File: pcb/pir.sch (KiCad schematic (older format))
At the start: 0 parts

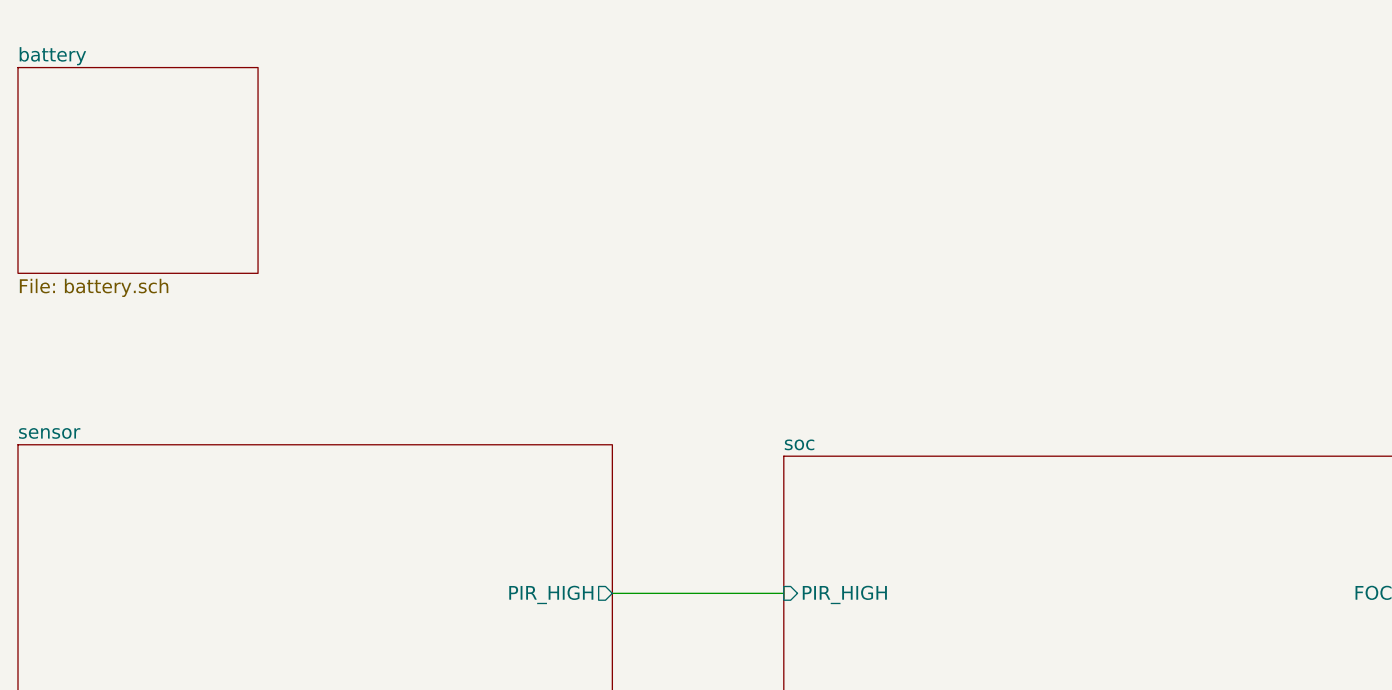
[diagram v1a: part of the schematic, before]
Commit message: User pushbutton
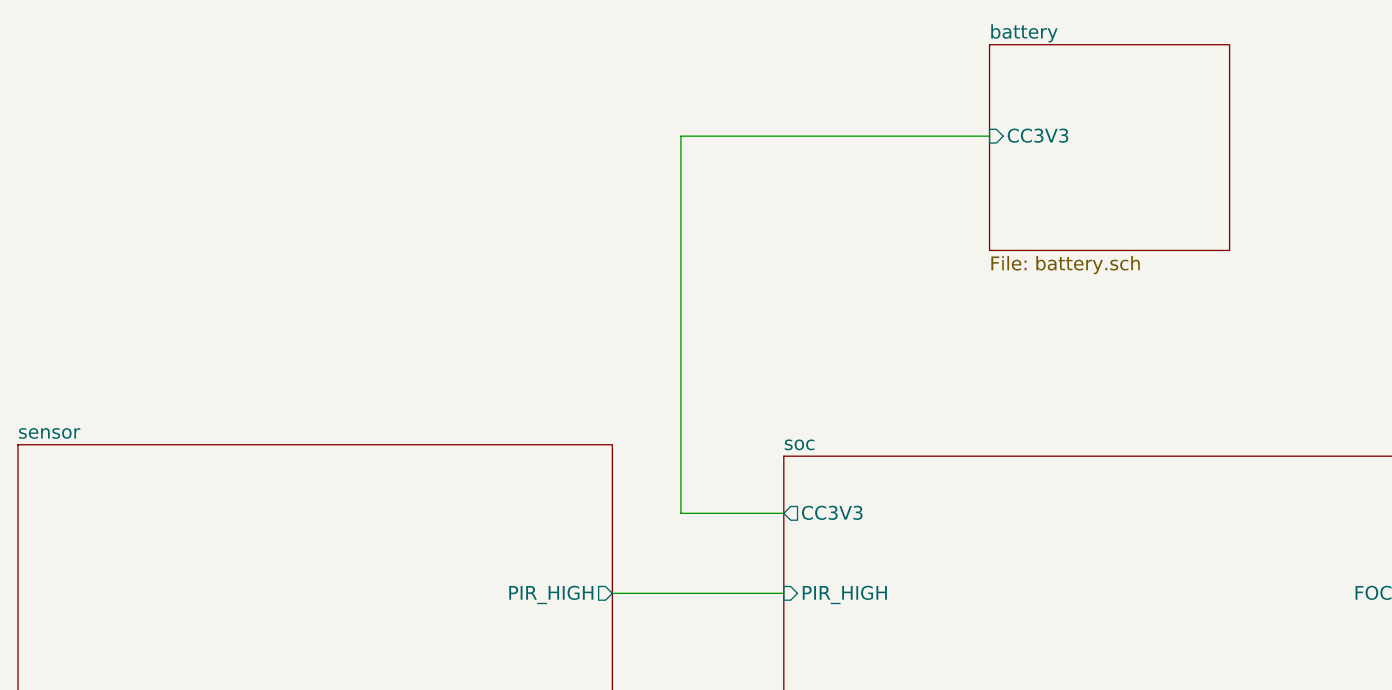
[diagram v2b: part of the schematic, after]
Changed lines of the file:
@@
 $EndSheet
 $Sheet
-S 1200 1250 1050 900
+S 5450 1150 1050 900
 U 5A769BAC
 F0 "battery" 60
 F1 "battery.sch" 60
+F2 "CC3V3" I L 5450 1550 60
 $EndSheet
 $Sheet
@@
 F4 "FOCUS" O R 7400 3550 60
 F5 "SHUTTER" O R 7400 4350 60
+F6 "CC3V3" O L 4550 3200 60
 $EndSheet
 Wire Wire Line
@@
 Wire Wire Line
 	7400 4350 8150 4350
+Wire Wire Line
+	4100 3200 4550 3200
+Wire Wire Line
+	4100 1550 4100 3200
+Wire Wire Line
+	4100 1550 5450 1550
 $EndSCHEMATC

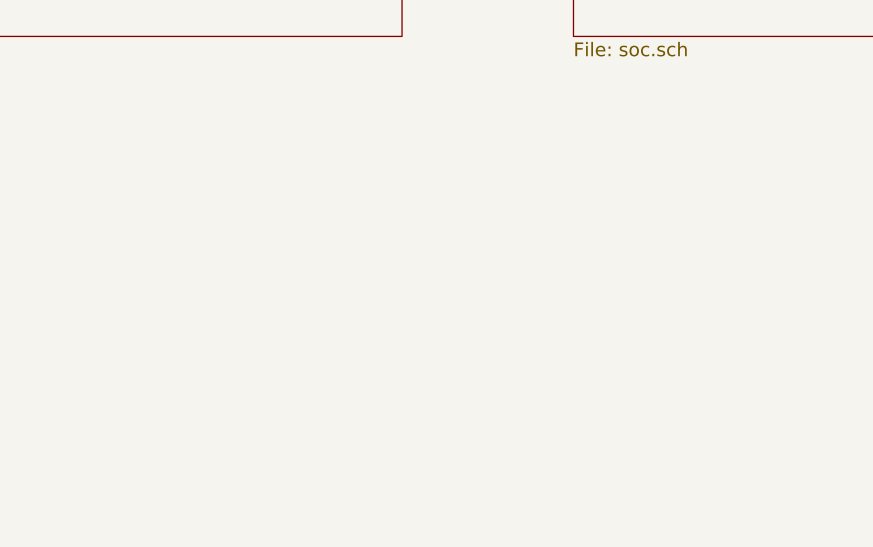
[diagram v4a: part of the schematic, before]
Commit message: Added E-Ink display
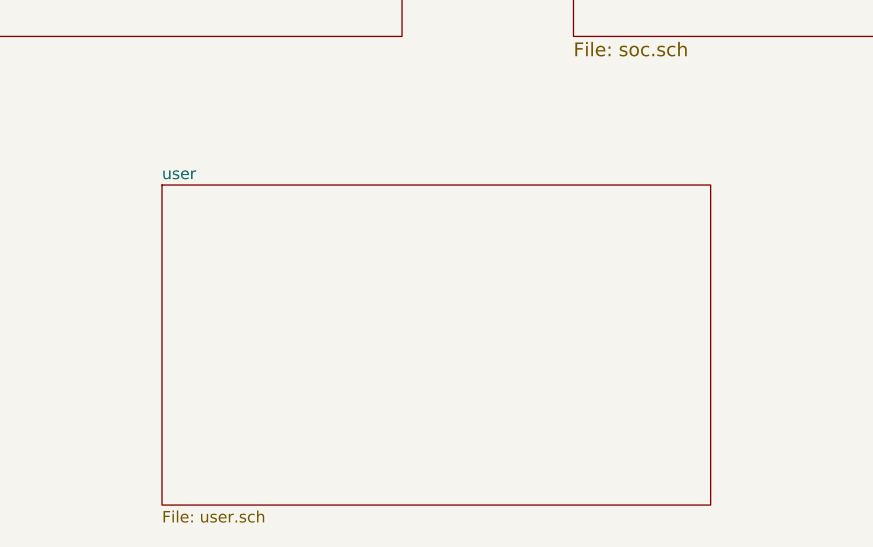
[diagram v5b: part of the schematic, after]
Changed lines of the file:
@@
 $Descr A4 11693 8268
 encoding utf-8
-Sheet 1 5
+Sheet 1 6
 Title ""
 Date ""
@@
 Wire Wire Line
 	4100 1550 5450 1550
+$Sheet
+S 2750 5500 2400 1400
+U 5A7EC53C
+F0 "user" 50
+F1 "user.sch" 50
+$EndSheet
 $EndSCHEMATC

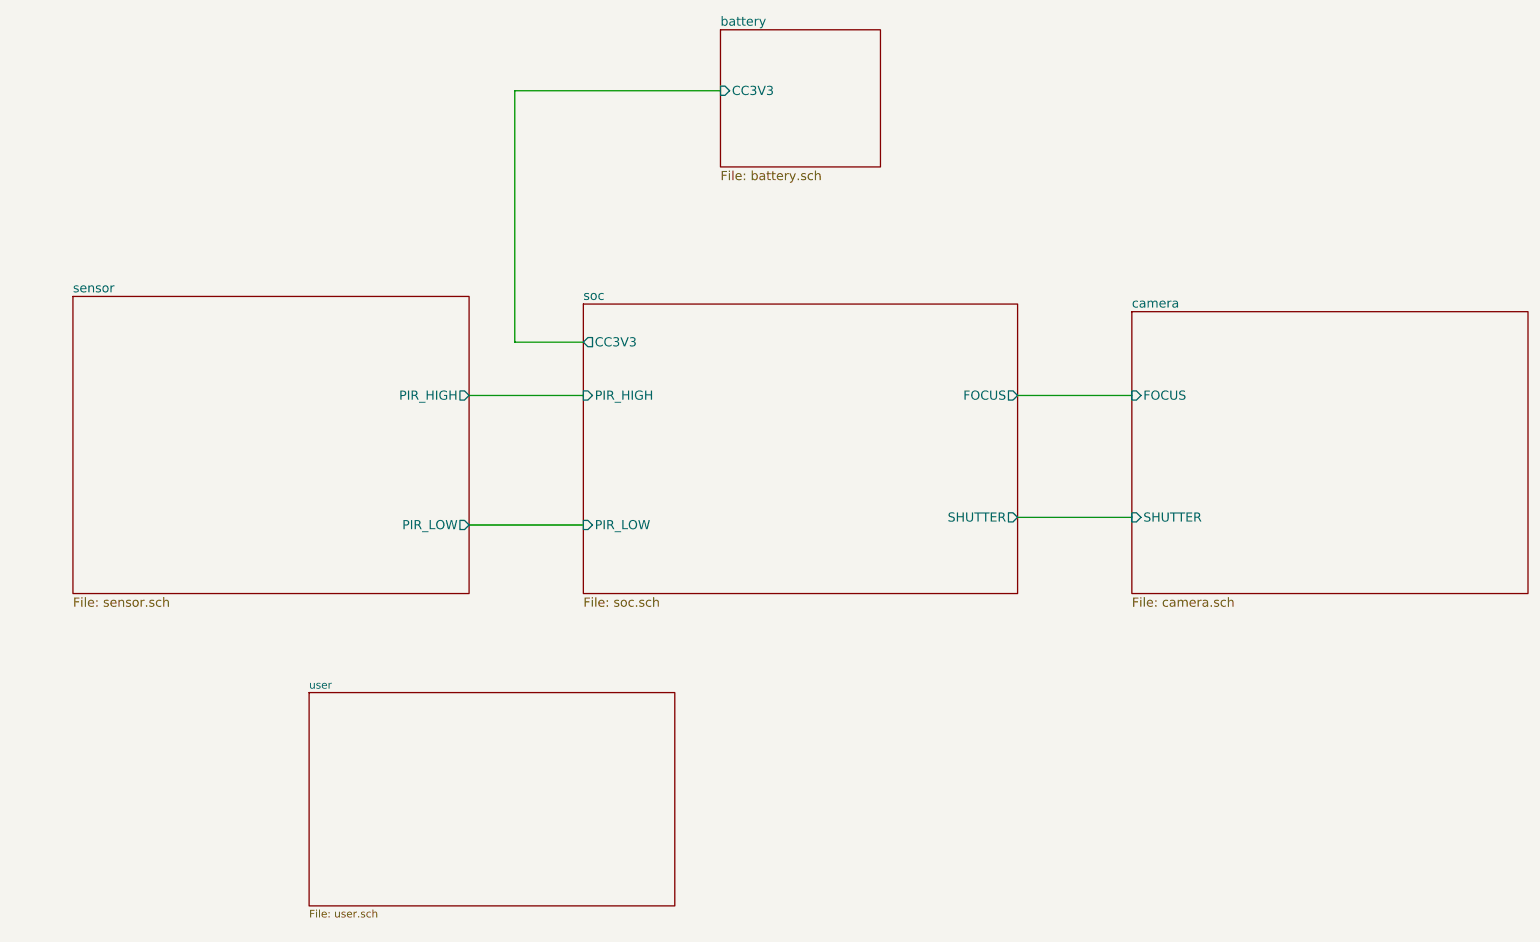
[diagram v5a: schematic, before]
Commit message: Added hierarchical signals for E-Ink
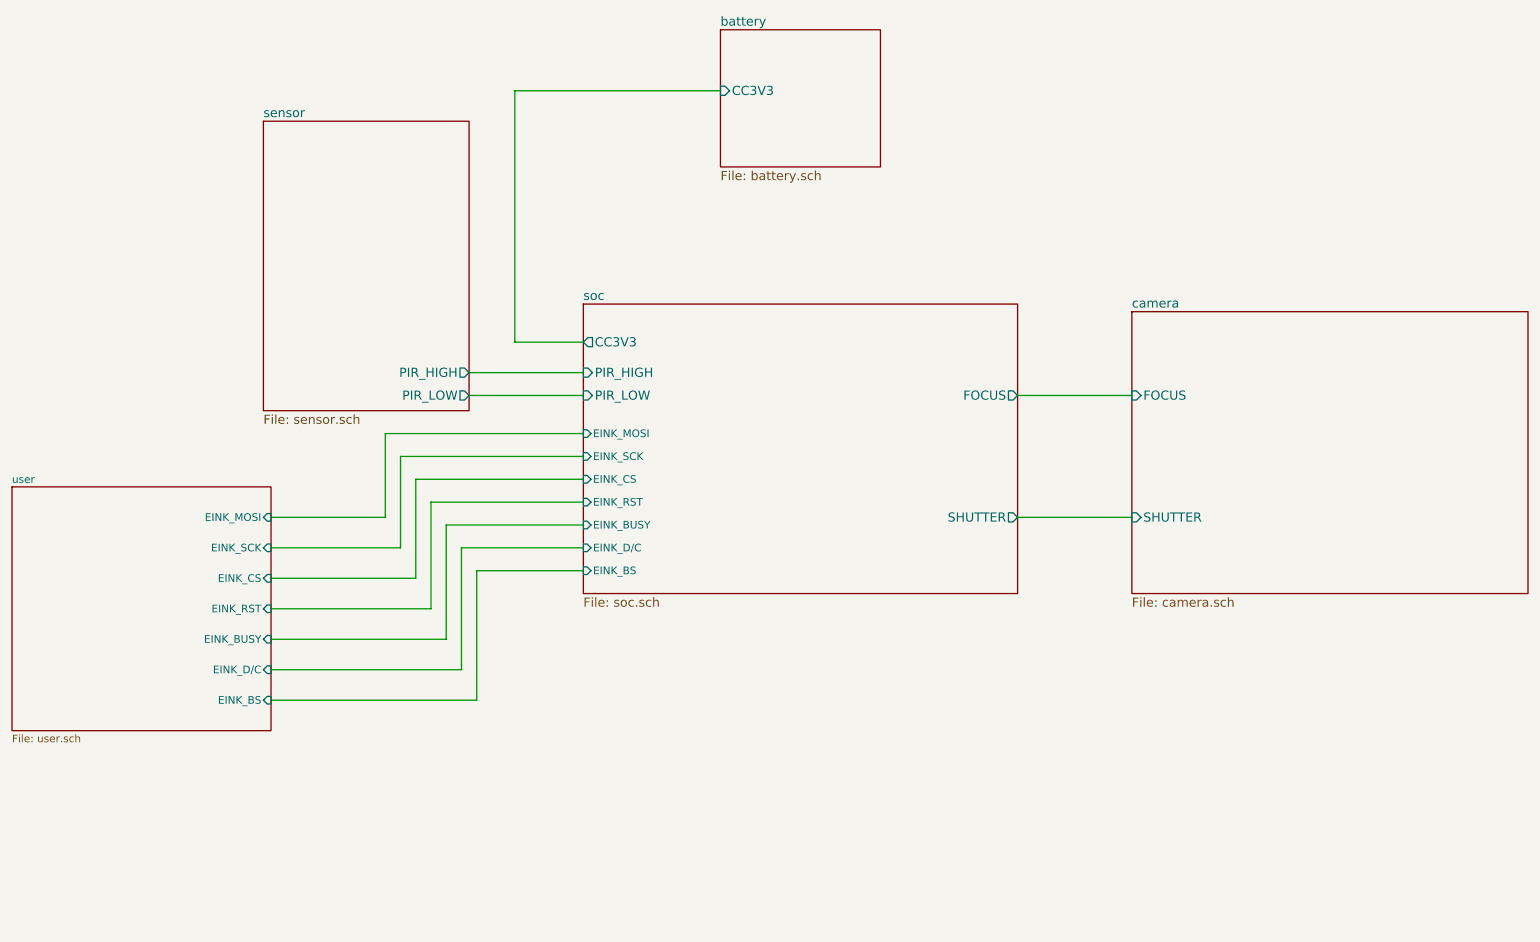
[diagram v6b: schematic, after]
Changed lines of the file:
@@
 $EndDescr
 $Sheet
-S 1200 2900 2600 1950
+S 2450 1750 1350 1900
 U 5A768E85
 F0 "sensor" 60
 F1 "sensor.sch" 60
-F2 "PIR_HIGH" O R 3800 3550 60
-F3 "PIR_LOW" O R 3800 4400 60
+F2 "PIR_HIGH" O R 3800 3400 60
+F3 "PIR_LOW" O R 3800 3550 60
 $EndSheet
 $Sheet
@@
 F0 "soc" 60
 F1 "soc.sch" 60
-F2 "PIR_HIGH" I L 4550 3550 60
-F3 "PIR_LOW" I L 4550 4400 60
+F2 "PIR_HIGH" I L 4550 3400 60
+F3 "PIR_LOW" I L 4550 3550 60
 F4 "FOCUS" O R 7400 3550 60
 F5 "SHUTTER" O R 7400 4350 60
 F6 "CC3V3" O L 4550 3200 60
+F7 "EINK_SCK" I L 4550 3950 50
+F8 "EINK_MOSI" I L 4550 3800 50
+F9 "EINK_CS" I L 4550 4100 50
+F10 "EINK_RST" I L 4550 4250 50
+F11 "EINK_BUSY" I L 4550 4400 50
+F12 "EINK_D/C" I L 4550 4550 50
+F13 "EINK_BS" I L 4550 4700 50
 $EndSheet
 Wire Wire Line
 	3800 3550 4550 3550
-Wire Wire Line
-	3800 4400 4550 4400
 $Sheet
 S 8150 3000 2600 1850
@@
 	4100 1550 5450 1550
 $Sheet
-S 2750 5500 2400 1400
+S 800  4150 1700 1600
 U 5A7EC53C
 F0 "user" 50
 F1 "user.sch" 50
+F2 "EINK_MOSI" I R 2500 4350 50
+F3 "EINK_SCK" I R 2500 4550 50
+F4 "EINK_CS" I R 2500 4750 50
+F5 "EINK_RST" I R 2500 4950 50
+F6 "EINK_BUSY" I R 2500 5150 50
+F7 "EINK_D/C" I R 2500 5350 50
+F8 "EINK_BS" I R 2500 5550 50
 $EndSheet
+Wire Wire Line
+	3800 3400 4550 3400
+Wire Wire Line
+	2500 4350 3250 4350
+Wire Wire Line
+	3250 4350 3250 3800
+Wire Wire Line
+	3250 3800 4550 3800
+Wire Wire Line
+	2500 4550 3350 4550
+Wire Wire Line
+	3350 4550 3350 3950
+Wire Wire Line
+	3350 3950 4550 3950
+Wire Wire Line
+	2500 4750 3450 4750
+Wire Wire Line
+	3450 4750 3450 4100
+Wire Wire Line
+	3450 4100 4550 4100
+Wire Wire Line
+	2500 4950 3550 4950
+Wire Wire Line
+	3550 4950 3550 4250
+Wire Wire Line
+	3550 4250 4550 4250
+Wire Wire Line
+	2500 5150 3650 5150
+Wire Wire Line
+	3650 5150 3650 4400
+Wire Wire Line
+	3650 4400 4550 4400
+Wire Wire Line
+	2500 5350 3750 5350
+Wire Wire Line
+	3750 5350 3750 4550
+Wire Wire Line
+	3750 4550 4550 4550
+Wire Wire Line
+	3850 5550 3850 4700
+Wire Wire Line
+	3850 4700 4550 4700
+Wire Wire Line
+	2500 5550 3850 5550
 $EndSCHEMATC

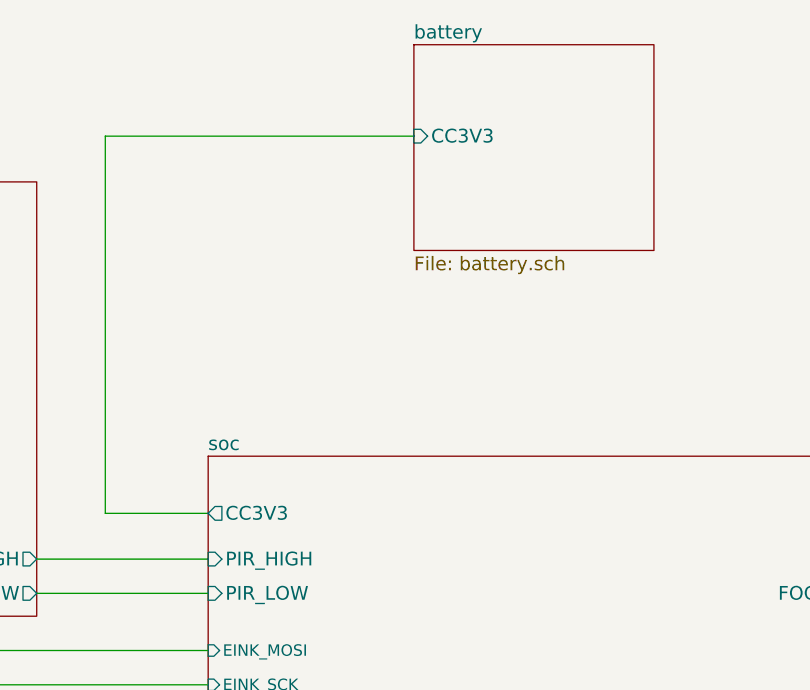
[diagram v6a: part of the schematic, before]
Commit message: Reverted to KiCad 4.0.7
+ Reworked debouncing for pushbuttons
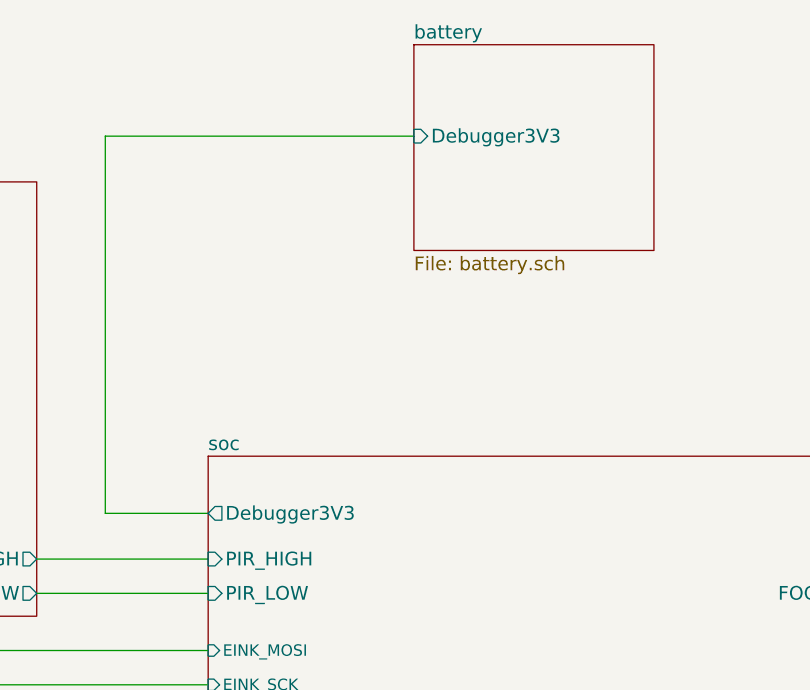
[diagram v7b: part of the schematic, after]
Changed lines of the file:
@@
-EESchema Schematic File Version 4
+EESchema Schematic File Version 2
+LIBS:power
 LIBS:pir-cache
-EELAYER 26 0
+EELAYER 25 0
 EELAYER END
 $Descr A4 11693 8268
@@
 F0 "battery" 60
 F1 "battery.sch" 60
-F2 "CC3V3" I L 5450 1550 60
+F2 "Debugger3V3" I L 5450 1550 60
 $EndSheet
 $Sheet
@@
 F4 "FOCUS" O R 7400 3550 60
 F5 "SHUTTER" O R 7400 4350 60
-F6 "CC3V3" O L 4550 3200 60
+F6 "Debugger3V3" O L 4550 3200 60
 F7 "EINK_SCK" I L 4550 3950 50
 F8 "EINK_MOSI" I L 4550 3800 50
